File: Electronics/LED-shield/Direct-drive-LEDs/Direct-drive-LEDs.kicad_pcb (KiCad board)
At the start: 2 copper layers, 43 parts, among them J1 Conn_01x11_Male, J2 Conn_01x02_Female, Q1 MMBT3904, Q2 BS170F, Q3 MMBT3904, Q4 BS170F, Q5 MMBT3904, Q6 BS170F, Q7 MMBT3904, Q8 BS170F, U1 OP275, U2 OP275

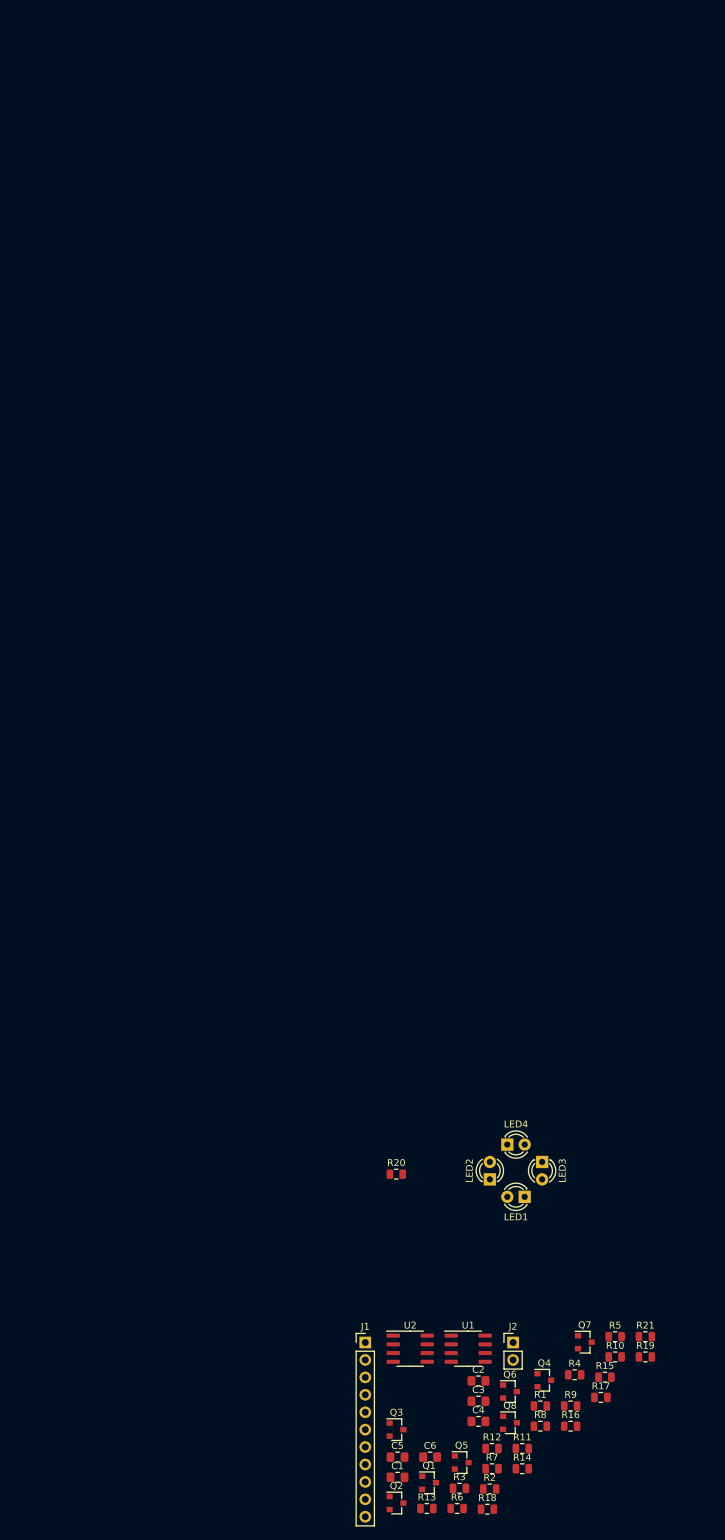
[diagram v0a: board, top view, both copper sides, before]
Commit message: Arduino MEGA shield for half-neuron WIP.
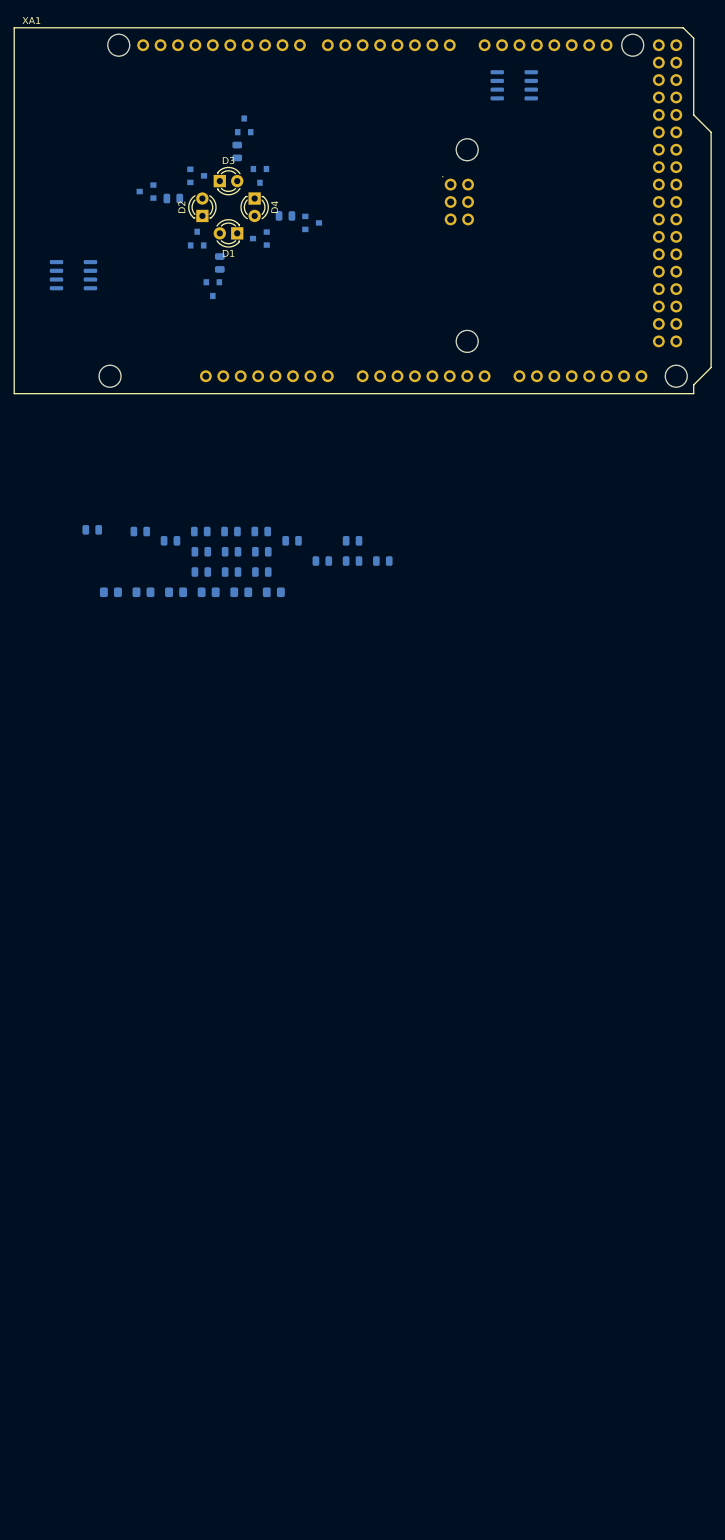
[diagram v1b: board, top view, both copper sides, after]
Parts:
- removed J1: Conn_01x11_Male, Connector_PinHeader_2.54mm:PinHeader_1x11_P2.54mm_Vertical
- removed J2: Conn_01x02_Female, Connector_PinHeader_2.54mm:PinHeader_1x02_P2.54mm_Vertical
- removed LED1, LED2, LED3, LED4: LED3MM, LED_THT:LED_D3.0mm
- added D1: LED, LED_THT:LED_D3.0mm, F.Cu at (87.6, -88.4)
- added D2: LED, LED_THT:LED_D3.0mm, F.Cu at (82.5, -90.9)
- added D3: LED, LED_THT:LED_D3.0mm, F.Cu at (85.1, -96.0)
- added D4: LED, LED_THT:LED_D3.0mm, F.Cu at (90.2, -93.5)
- added XA1: Arduino_Mega2560_Shield, arduino:Arduino_Mega2560_Shield, F.Cu at (55.1, -65.0)
- C1, C2, C3, C4, C5, C6, Q1, Q2, Q3, Q4, Q5, Q6, Q7, Q8, R1, R10, R11, R12, R13, R14, R15, R16, R17, R18, R19, R2, R20, R21, R3, R4, R5, R6, R7, R8, R9, U1, U2: moved to B.Cu
- moved Q5 197.5 mm to (88.6, -104.1), turned to 90 degrees
- moved R11 189.2 mm to (78.3, -93.5), turned to 180 degrees
- moved Q2 185.4 mm to (90.9, -87.6), turned to 180 degrees
- moved Q8 185.4 mm to (90.9, -96.8), turned to 270 degrees
- moved R6 184.9 mm to (85.1, -84.1), turned to 270 degrees
- moved U2 184.8 mm to (128.0, -110.0)
- moved Q3 184.1 mm to (74.4, -94.5), turned to 180 degrees
- moved Q6 183.0 mm to (81.8, -96.8)
- moved Q1 176.9 mm to (84.1, -80.3), turned to 270 degrees
- moved Q4 174.0 mm to (81.8, -87.6), turned to 90 degrees
- moved R21 171.6 mm to (94.7, -90.9)
- moved Q7 168.0 mm to (98.6, -89.9)
- moved U1 166.8 mm to (63.8, -82.3)
- moved R20 150.9 mm to (87.6, -100.3), turned to 90 degrees
- moved R14 147.5 mm to (73.5, -44.9)
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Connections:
- net GND renamed PhotoE
- R5 pad 1: Net-(J1-Pad6) -> photoC

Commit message: Minor PCB mods WIP.
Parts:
- added H1: MountingHole, MountingHole:MountingHole_2.1mm, F.Cu at (95.0, -84.0)
- added H2: MountingHole, MountingHole:MountingHole_2.1mm, F.Cu at (78.0, -101.0)
- added J1: Conn_01x02_Male, Connector_PinHeader_2.54mm:PinHeader_1x02_P2.54mm_Vertical, F.Cu at (112.0, -47.0)
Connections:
- net PhotoE renamed GND

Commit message: More PCB WIP.
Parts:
- H1, H2: footprint MountingHole:MountingHole_2.1mm -> MountingHole:MountingHole_4.3mm_M4
- U1, U2: value OP275 -> TLC2722
- moved C4 82.5 mm to (102.6, -111.5), turned to 180 degrees
- moved C3 82.0 mm to (113.0, -108.2), turned to 270 degrees
- moved R1 79.7 mm to (113.5, -112.3), turned to 90 degrees
- moved C1 78.9 mm to (116.8, -111.3)
- moved R2 76.1 mm to (116.8, -109.0)
- moved C5 75.7 mm to (106.4, -108.2), turned to 270 degrees
- moved R13 73.6 mm to (108.5, -112.3), turned to 90 degrees
- moved R7 72.6 mm to (111.0, -112.3), turned to 90 degrees
- moved R15 71.4 mm to (108.5, -108.3), turned to 270 degrees
- moved R14 70.7 mm to (102.9, -109.2), turned to 180 degrees
- moved R12 68.8 mm to (105.9, -112.3), turned to 90 degrees
- moved R8 68.0 mm to (111.0, -108.3), turned to 270 degrees
- moved C2 62.7 mm to (97.0, -96.0)
- moved R16 61.3 mm to (103.7, -102.4)
- moved R18 57.4 mm to (65.3, -96.2), turned to 270 degrees
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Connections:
- U1 pad 4: (no net) -> GND
- U1 pad 8: (no net) -> +5V
- U2 pad 4: (no net) -> GND
- U2 pad 8: (no net) -> +5V
- XA1 pad D13: PWMin3 -> Net-(XA1-PadD13)
- XA1 pad D2: Net-(XA1-PadD2) -> PWMin0
- XA1 pad D23: LEDon1 -> Net-(XA1-PadD23)
- XA1 pad D24: LEDon2 -> LEDon1
- XA1 pad D25: LEDon3 -> Net-(XA1-PadD25)
- XA1 pad D26: Net-(XA1-PadD26) -> LEDon2
- XA1 pad D28: Net-(XA1-PadD28) -> LEDon3
- XA1 pad D3: Net-(XA1-PadD3) -> PWMin1
- XA1 pad D4: Net-(XA1-PadD4) -> PWMin2
- XA1 pad D44: PWMin2 -> Net-(XA1-PadD44)
- XA1 pad D45: PWMin1 -> Net-(XA1-PadD45)
- XA1 pad D46: PWMin0 -> Net-(XA1-PadD46)
- XA1 pad D5: Net-(XA1-PadD5) -> PWMin3
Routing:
- net +5V: track 0.00 -> 41.1 mm
- net photoC: track 0.00 -> 6.71 mm
- net Net-(C4-Pad1): track 0.00 -> 4.66 mm
- net Net-(C1-Pad1): track 0.00 -> 4.63 mm
- net Net-(C5-Pad1): track 0.00 -> 4.22 mm
- net Net-(C3-Pad1): track 0.00 -> 4.22 mm
- net Net-(D4-Pad2): track 0.00 -> 3.56 mm
- net Net-(D3-Pad2): track 0.00 -> 3.38 mm
- net Net-(D1-Pad2): track 0.00 -> 3.38 mm
- net Net-(D2-Pad2): track 0.00 -> 3.30 mm
- net Net-(Q6-Pad1): track 0.00 -> 2.89 mm
- net Net-(Q8-Pad1): track 0.00 -> 2.63 mm
- net Net-(D4-Pad1): track 0.00 -> 2.62 mm
- net Net-(D3-Pad1): track 0.00 -> 2.62 mm
- net Net-(D2-Pad1): track 0.00 -> 2.62 mm
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
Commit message: More PCB WIP...
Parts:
- removed H1, H2: MountingHole, MountingHole:MountingHole_4.3mm_M4
- C1, C2, C3, C4, C5, C6, Q1, Q2, Q3, Q4, Q5, Q6, Q7, Q8, R1, R10, R11, R12, R13, R14, R15, R16, R17, R18, R19, R2, R20, R21, R3, R4, R5, R6, R7, R8, R9, U1, U2: moved to F.Cu
- XA1: footprint arduino:Arduino_Mega2560_Shield -> reprapltd-kicad:Arduino_Mega2560_Shield
- moved C2 254.5 mm to (35.3, 150.9), turned to 180 degrees
- moved R16 254.4 mm to (62.2, 148.6)
- moved R17 254.0 mm to (42.6, 148.6)
- moved U1 253.6 mm to (35.1, 146.7), turned to 0 degrees
- moved R14 252.7 mm to (48.5, 137.6), turned to 270 degrees
- moved R15 252.7 mm to (50.8, 137.7)
- moved R2 252.7 mm to (61.5, 137.6), turned to 270 degrees
- moved C3 252.3 mm to (56.4, 137.7)
- moved C5 251.4 mm to (53.8, 137.7)
- moved R8 251.2 mm to (59.2, 137.5)
- moved C4 251.0 mm to (47.5, 133.3)
- moved R1 250.6 mm to (58.9, 132.3)
- moved R12 250.6 mm to (51.3, 132.3)
- moved R13 250.6 mm to (53.8, 132.3)
- moved R7 250.6 mm to (56.4, 132.3)
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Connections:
- R16 pad 1: Net-(R14-Pad2) -> Net-(R16-Pad1)
- R2 pad 2: Net-(R2-Pad2) -> Net-(R16-Pad1)
- R3 pad 1: Net-(R2-Pad2) -> Net-(R14-Pad2)
- U1 pad 3: Net-(R2-Pad2) -> Net-(R14-Pad2)
- U1 pad 5: Net-(R8-Pad2) -> Net-(R15-Pad2)
- U1 pad 6: Net-(Q3-Pad2) -> Net-(Q7-Pad2)
- U1 pad 7: Net-(Q3-Pad1) -> Net-(Q7-Pad1)
- U2 pad 1: Net-(Q7-Pad1) -> Net-(Q3-Pad1)
- U2 pad 2: Net-(Q7-Pad2) -> Net-(Q3-Pad2)
- U2 pad 3: Net-(R15-Pad2) -> Net-(R8-Pad2)
- U2 pad 5: Net-(R14-Pad2) -> Net-(R16-Pad1)
- XA1 pad 5V3: +5V -> Net-(XA1-Pad5V3)
- XA1 pad 5V4: +5V -> Net-(XA1-Pad5V3)
- XA1 pad D10: Net-(XA1-PadD10) -> PWMin0
- XA1 pad D11: Net-(XA1-PadD11) -> PWMin1
- XA1 pad D12: Net-(XA1-PadD12) -> PWMin2
- XA1 pad D13: Net-(XA1-PadD13) -> PWMin3
- XA1 pad D2: PWMin0 -> Net-(XA1-PadD2)
- XA1 pad D22: LEDon0 -> Net-(XA1-PadD22)
- XA1 pad D24: LEDon1 -> LEDon0
- XA1 pad D26: LEDon2 -> LEDon1
- XA1 pad D28: LEDon3 -> LEDon2
- XA1 pad D3: PWMin1 -> Net-(XA1-PadD3)
- XA1 pad D30: Net-(XA1-PadD30) -> LEDon3
- XA1 pad D4: PWMin2 -> Net-(XA1-PadD4)
- XA1 pad D5: PWMin3 -> Net-(XA1-PadD5)
- XA1 pad GND1: GND -> Net-(XA1-PadGND1)
- XA1 pad GND2: GND -> Net-(XA1-PadGND2)
- XA1 pad GND5: GND -> Net-(XA1-PadGND5)
- XA1 pad GND6: GND -> Net-(XA1-PadGND5)
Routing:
- net +5V: track 41.1 -> 114.1 mm
- net Net-(Q3-Pad2): track 1.99 -> 40.9 mm
- net Net-(R14-Pad2): track 0.00 -> 32.9 mm
- net Net-(D3-Pad1): track 2.62 -> 28.9 mm
- net Net-(R15-Pad2): track 0.00 -> 20.9 mm
- net Net-(Q7-Pad2): track 1.98 -> 22.5 mm, vias 0 -> 1
- net Net-(R8-Pad2): track 0.00 -> 20.5 mm
- net Net-(D1-Pad1): track 2.62 -> 21.0 mm
- net Net-(R16-Pad1): track 0.00 -> 14.2 mm
- net Net-(Q7-Pad1): track 0.00 -> 12.8 mm, vias 0 -> 1
- net Net-(D4-Pad1): track 2.62 -> 14.7 mm
- net Net-(D2-Pad2): track 3.30 -> 15.1 mm, vias 0 -> 1
- net Net-(Q5-Pad2): track 1.90 -> 12.3 mm, vias 0 -> 1
- net Net-(D1-Pad2): track 3.38 -> 11.9 mm, vias 0 -> 1
- net Net-(Q5-Pad1): track 0.00 -> 7.63 mm, vias 0 -> 1
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
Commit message: First finished PCB.
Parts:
- moved Q2 26.9 mm to (108.3, 160.5)
- moved Q4 26.9 mm to (108.3, 164.6)
- moved Q6 26.9 mm to (108.3, 172.7)
- moved R10 26.9 mm to (112.9, 163.6)
- moved R18 26.9 mm to (113.0, 170.8)
- moved Q8 26.9 mm to (108.3, 168.6)
- moved R19 26.9 mm to (113.0, 166.9)
- moved R4 26.9 mm to (112.9, 160.5)
- moved R9 26.3 mm to (64.1, 167.6), turned to 0 degrees
- moved R3 22.4 mm to (41.4, 164.6), turned to 90 degrees
- moved C3 22.1 mm to (56.4, 159.8)
- moved C4 22.1 mm to (47.5, 155.4)
- moved C5 22.1 mm to (53.8, 159.8)
- moved D1 22.1 mm to (92.7, 158.5)
- moved D2 22.1 mm to (97.8, 161.0)
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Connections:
- XA1 pad D24: LEDon0 -> Net-(XA1-PadD24)
- XA1 pad D26: LEDon1 -> Net-(XA1-PadD26)
- XA1 pad D28: LEDon2 -> Net-(XA1-PadD28)
- XA1 pad D30: LEDon3 -> Net-(XA1-PadD30)
- XA1 pad D46: Net-(XA1-PadD46) -> LEDon0
- XA1 pad D48: Net-(XA1-PadD48) -> LEDon1
- XA1 pad D50: Net-(XA1-PadD50) -> LEDon2
- XA1 pad D52: Net-(XA1-PadD52) -> LEDon3
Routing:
- net Net-(Q1-Pad2): track 5.18 -> 79.2 mm, vias 1 -> 2
- net Net-(Q1-Pad1): track 3.10 -> 75.3 mm, vias 1 -> 2
- net Net-(Q7-Pad2): track 22.5 -> 89.3 mm, vias 1 -> 2
- net Net-(Q7-Pad1): track 12.8 -> 76.8 mm, vias 1 -> 2
- net Net-(Q5-Pad2): track 12.3 -> 59.9 mm, vias 1 -> 2
- net Net-(R15-Pad2): track 20.9 -> 59.1 mm
- net Net-(Q5-Pad1): track 7.63 -> 44.6 mm, vias 1 -> 2
- net GND: track 0.00 -> 27.4 mm, vias 0 -> 7
- net PWMin0: track 0.00 -> 24.9 mm
- net +5V: track 114.1 -> 137.2 mm, vias 0 -> 2
- net PWMin3: track 2.77 -> 24.9 mm
- net PWMin2: track 2.77 -> 24.9 mm
- net PWMin1: track 2.77 -> 24.9 mm
- net Net-(Q3-Pad1): track 0.00 -> 19.4 mm, vias 0 -> 2
- net Net-(R14-Pad2): track 32.9 -> 13.7 mm
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- added copper zone on F.Cu, net GND

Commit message: PCB GERBERS.
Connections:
- XA1 pad 5V3: Net-(XA1-Pad5V3) -> +5V
- XA1 pad 5V4: Net-(XA1-Pad5V3) -> +5V
- XA1 pad GND1: Net-(XA1-PadGND1) -> GND
- XA1 pad GND2: Net-(XA1-PadGND2) -> GND
- XA1 pad GND5: Net-(XA1-PadGND5) -> GND
- XA1 pad GND6: Net-(XA1-PadGND5) -> GND
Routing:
- net +5V: track 137.2 -> 139.7 mm
- net Net-(XA1-PadGND5): track 2.54 -> 0.00 mm
- net Net-(XA1-Pad5V3): track 2.54 -> 0.00 mm
- net GND: track 27.4 -> 30.0 mm
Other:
- board outline added: 101.6 x 53.3 mm

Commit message: Now with better resistance values...
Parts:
- R5: value 3K3 -> 560R

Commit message: WIP on pure electronic version
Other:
- net class Default removed
